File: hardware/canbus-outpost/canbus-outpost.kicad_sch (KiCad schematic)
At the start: 117 parts, among them J1 SERVO, J10 RJ45, J11 SWD, J12 UART, J13 RJ45, J14 GPIO, J2 DCC_SIG, J3 BOOSTER, J4 TRACK1, J5 TRACK2, J6 TRACK3, J7 TRACK4, J8 VDC, J9 USB, SW1 BUTTON, SW2 BUTTON, U1 W25Q32JVSS, U10 ISO7720D, U11 L78L05_SO8, U12 ISO7720D, U13 ISO7720D, U14 ISO7720D, U2 RP2350A, U3 TPS5430DDA, U4 SN65HVD230, U5 XC6206PxxxMR, U6 TLV3202, U7 TLV3202, U8 TLV3202, U9 TLV3202, Y1 ABM8-272-T3

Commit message: fix(hardware): fix railcom circuits
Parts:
- removed C23, C24: 100uF, Library:CP_Elec_6.3x7.7, symbol Library:C_Polarized
- removed D4, D5: SS54, Library:D_SMA, symbol Library:D
- removed J12: UART, Library:PinHeader_1x03_P2.54mm_Vertical, symbol Library:Conn_01x03_Pin
- removed R12, R13: 220R, Library:R_0402_1005Metric, symbol Library:R
- removed R22, R23, R24, R25, R26, R27, R28, R29: 10K, Library:R_0402_1005Metric, symbol Library:R
- added C23, C35, C36, C37, C38, C39: 100nF, Library:C_0402_1005Metric, symbol Library:C
- added D5: 1N5819WS, Diode_SMD:D_SOD-323, symbol Diode:1N5819WS
- added R31, R32, R33, R34, R37, R39, R41: 1K, Library:R_0402_1005Metric, symbol Library:R
- added R35: 2.2K, Library:R_1206_3216Metric, symbol Library:R
- added R36: 4.7K, Library:R_0402_1005Metric, symbol Library:R
- added R38, R40, R42: 330K, Library:R_0402_1005Metric, symbol Library:R
- added U15: TLP290(GB-TP,SE), Package_SO:SOIC-4_4.55x2.6mm_P1.27mm, symbol Isolator:LTV-354T
- J14: footprint Library:PinHeader_1x04_P2.54mm_Vertical -> Connector_PinHeader_2.54mm:PinHeader_1x08_P2.54mm_Vertical; symbol Library:Conn_01x04_Pin -> Connector:Conn_01x08_Pin
- J4: value TRACK1 -> TRACK4
- J5: value TRACK2 -> TRACK3
- J6: value TRACK3 -> TRACK2
- J7: value TRACK4 -> TRACK1
- R11, R30: value 220R -> 1K; LCSC C25091 -> C11702
- R14: value 270K -> 330K; LCSC C25770 -> C25778
- R16: value 820R -> 330K; LCSC C25924 -> C25778
- R17: value 33K -> 1K; LCSC C25779 -> C11702
- U1: LCSC C82344 -> C179173
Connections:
- net RC_REF_L is gone; now on net RC_REF_H: R14.2, R15.1, U6.6 (-), U7.6 (-), U8.6 (-), U9.6 (-)
- net +3.3V: now also C35.1, R36.1
- net +5V: now also D5.1 (K); no longer J9.1 (Pin_1)
- net +5VR: now also R16.1, C36.1, C37.1, C38.1, C39.1, R38.1, R40.1, R42.1
- net BOOSTER_L: now also R35.2
- net BOOSTER_R: now also U6.3 (+), U6.4 (V-), U7.3 (+), U7.4 (V-), U8.3 (+), U8.4 (V-), U9.3 (+), U9.4 (V-), C23.2, C36.2, C37.2, C38.2, C39.2, U15.2; no longer R16.1
- net CAN_H: now also U4.7 (CANH); no longer U4.6 (CANL)
- net CAN_L: now also U4.6 (CANL); no longer U4.7 (CANH)
- net GND: now also C35.2, U15.3
- net RC_REF_H: now also C23.1; no longer R16.2, R17.1, U6.3 (+), U7.3 (+), U8.3 (+), U9.3 (+)
- net TRACK_R1: now also R34.1, R39.1; no longer U9.2 (-), U9.5 (+)
- net TRACK_R2: now also R33.1, R37.1; no longer U8.2 (-), U8.5 (+)
- net TRACK_R3: now also R17.1, R32.1; no longer U7.2 (-), U7.5 (+)
- net TRACK_R4: now also R31.1, R41.1; no longer U6.2 (-), U6.5 (+)
- net GPIO8: now reaches U2.12 (GPIO8)
- net GPIO8: now also J14.5 (Pin_5)
- net GPIO9: now reaches U2.13 (GPIO9)
- net GPIO9: now also J14.6 (Pin_6)
- net GPIO10: now reaches U2.14 (GPIO10)
- net GPIO10: now also J14.7 (Pin_7)
- net GPIO11: now reaches U2.15 (GPIO11)
- net GPIO11: now also J14.8 (Pin_8)
- net CUTOUT_SIGNAL: now reaches U2.43 (GPIO29_ADC3)
- net CUTOUT_SIGNAL: now also R36.2, U15.4
- removed net GNDA: R17.2, U6.4 (V-), U7.4 (V-), U8.4 (V-), U9.4 (V-)
- new net: R16.2, R17.2, U7.2 (-)
- new net: R37.2, R38.2, U8.2 (-)
- new net: D5.2 (A), J9.1 (Pin_1)
- new net: R35.1, U15.1
- new net: R39.2, R40.2, U9.2 (-)
- new net: R41.2, R42.2, U6.2 (-)
- new net: R33.2, U8.5 (+)
- new net: R31.2, U6.5 (+)
- new net: R34.2, U9.5 (+)
- new net: R32.2, U7.5 (+)
- no-connect marks 7 -> 6
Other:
- note added: "Railcom Cutout Signal"
- moved on the sheet: J9, U6A, U6B, U6C, U7A, U7B, U7C, U8A, U8B, U8C, U9A, U9B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

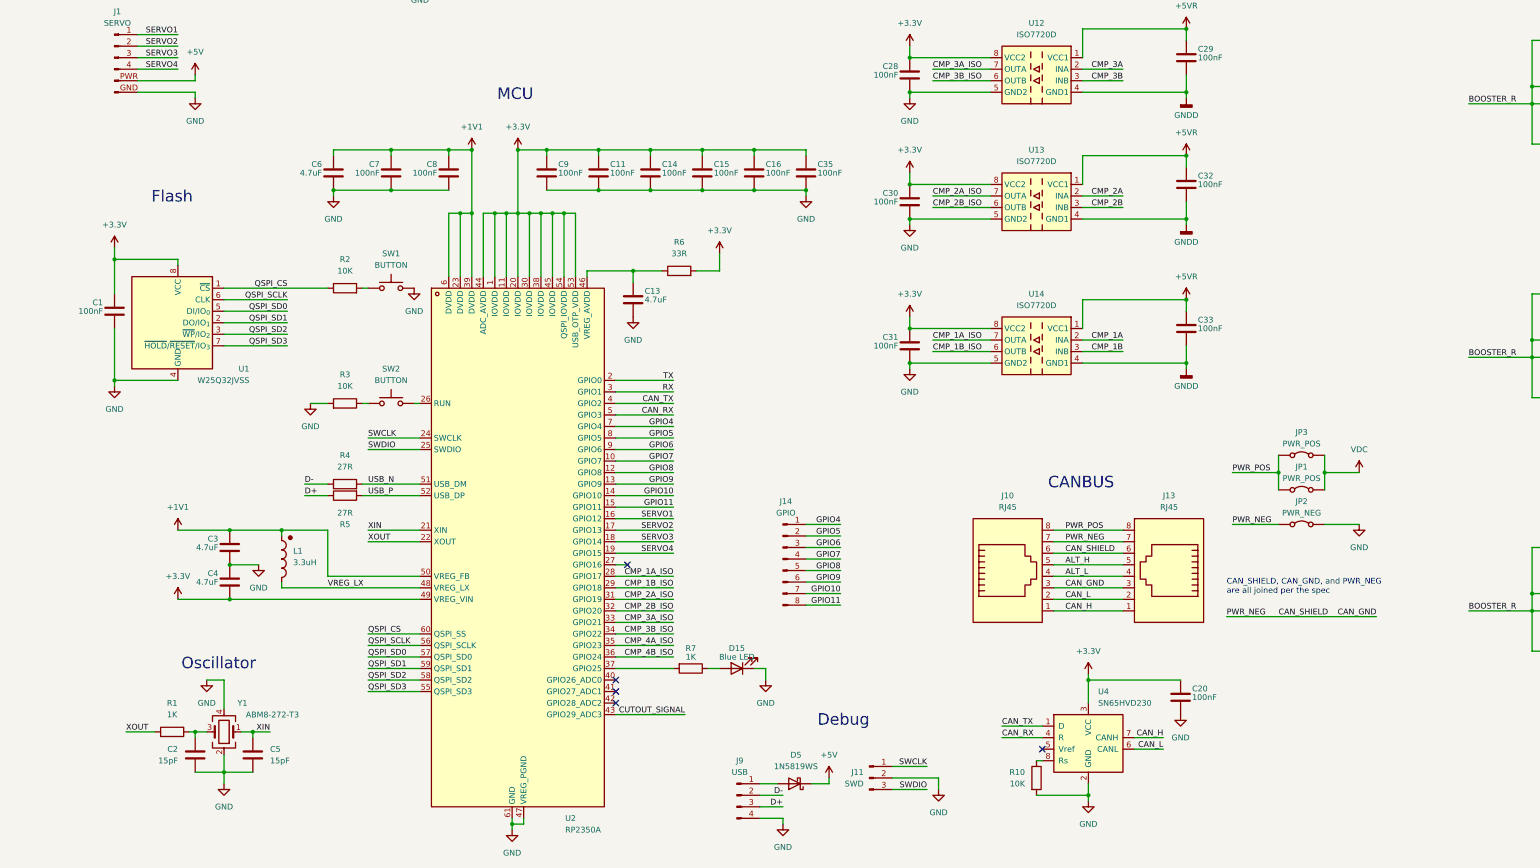
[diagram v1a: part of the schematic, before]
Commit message: feat: add usb jack for flashing
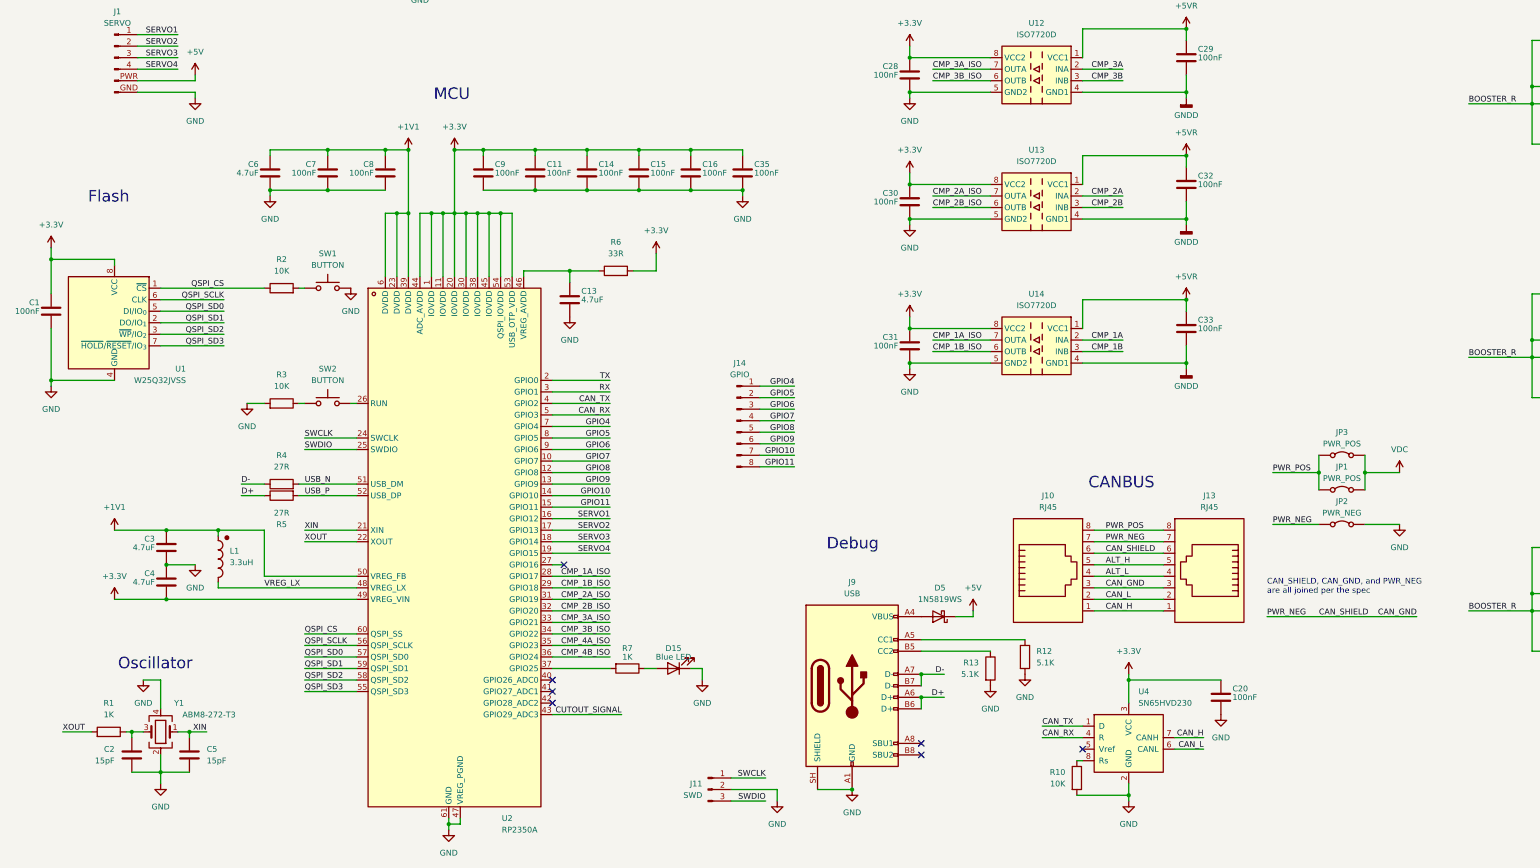
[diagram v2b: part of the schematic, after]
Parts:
- added R12, R13: 5.1K, Library:R_0402_1005Metric, symbol Library:R
- J9: footprint Library:PinHeader_1x04_P2.54mm_Vertical -> Connector_USB:USB_C_Receptacle_GCT_USB4115-03-C; symbol Library:Conn_01x04_Pin -> Connector:USB_C_Receptacle_USB2.0_16P; LCSC (none) -> C720628
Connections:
- net D+: now also J9.A6 (D+), J9.B6 (D+); no longer J9.3 (Pin_3)
- net D-: now also J9.A7 (D-), J9.B7 (D-); no longer J9.2 (Pin_2)
- net GND: now also J9.A1 (GND), J9.A12 (GND), J9.B1 (GND), J9.B12 (GND), J9.SH (SHIELD), R12.2, R13.2; no longer J9.4 (Pin_4)
- net at D5.2 (A): now also J9.A4 (VBUS), J9.A9 (VBUS), J9.B4 (VBUS), J9.B9 (VBUS); no longer J9.1 (Pin_1)
- new net: J9.A5 (CC1), R12.1
- new net: J9.B5 (CC2), R13.1
- no-connect marks 6 -> 8
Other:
- moved on the sheet: C1, C11, C13, C14, C15, C16, C2, C20, C3, C35, C4, C5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

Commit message: feat: add SSSB LED signal header
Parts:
- added C24: 100nF, Library:C_0402_1005Metric, symbol Library:C
- added F2: 750mA, Fuse:Fuse_1206_3216Metric, symbol Library:Polyfuse
- added J12: GND, Connector_PinHeader_2.54mm:PinHeader_1x02_P2.54mm_Vertical, symbol Library:Conn_01x02_Pin
- added J15: LIGHTS, Library:PinHeader_1x03_P2.54mm_Vertical, symbol Library:Conn_01x03_Pin
- added R22: 33R, Library:R_0402_1005Metric, symbol Library:R
- added U16: 74AHCT1G125, Package_TO_SOT_SMD:SOT-23-5, symbol 74xGxx:74AHCT1G125
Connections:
- net +5V: now also C24.1, F2.1, U16.5 (VCC)
- net GND: now also C24.2, J12.1 (Pin_1), J12.2 (Pin_2), J15.3 (Pin_3), U16.1, U16.3 (GND)
- net LIGHTS: now reaches U2.42 (GPIO28_ADC2)
- net LIGHTS: now also U16.2
- new net: R22.1, U16.4
- new net: J15.1 (Pin_1), R22.2
- new net: F2.2, J15.2 (Pin_2)
- no-connect marks 8 -> 7
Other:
- note added: "Connectors"
- note added: "Lights"
- note removed: "Rail Connectors"
- moved on the sheet: C10, C12, C17, C18, C19, C21, D1, D2, D3, F1, J1, J14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
